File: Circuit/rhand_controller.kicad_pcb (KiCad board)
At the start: 2 copper layers, 100 x 100 mm, 39 parts, among them P1 BLUETOOTH, P10 LV_ADC, P11 LW_ADC, P12 RU_ADC, P13 RV_ADC, P14 RW_ADC, P2 CONN_01X06, P3 Wall, P4 CW, P5 Enable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

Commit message: 実態配線図完了
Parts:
- moved D1 10.2 mm to (83.0, 104.7), turned to 270 degrees
- moved R5 8.90 mm to (90.5, 110.4), turned to 180 degrees
- moved P2 2.67 mm to (79.8, 74.0)
- moved R7 2.05 mm to (105.0, 124.5)
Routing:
- net GND: track 418.2 -> 558.3 mm
- net +3V3: track 358.1 -> 386.8 mm, vias 0 -> 2
- net Net-(R5-Pad1): track 0.11 -> 4.50 mm
- net /SWDIO: track 0.00 -> 3.63 mm
- net Net-(D1-Pad2): track 0.00 -> 3.22 mm
- net /SWO: track 0.00 -> 2.96 mm
- net /315MHz_RXD: track 0.00 -> 2.20 mm
- net /NRST: track 4.76 -> 6.84 mm
- added copper zone on B.Cu, net /NRST
- added copper zone on B.Cu, net /SWCLK

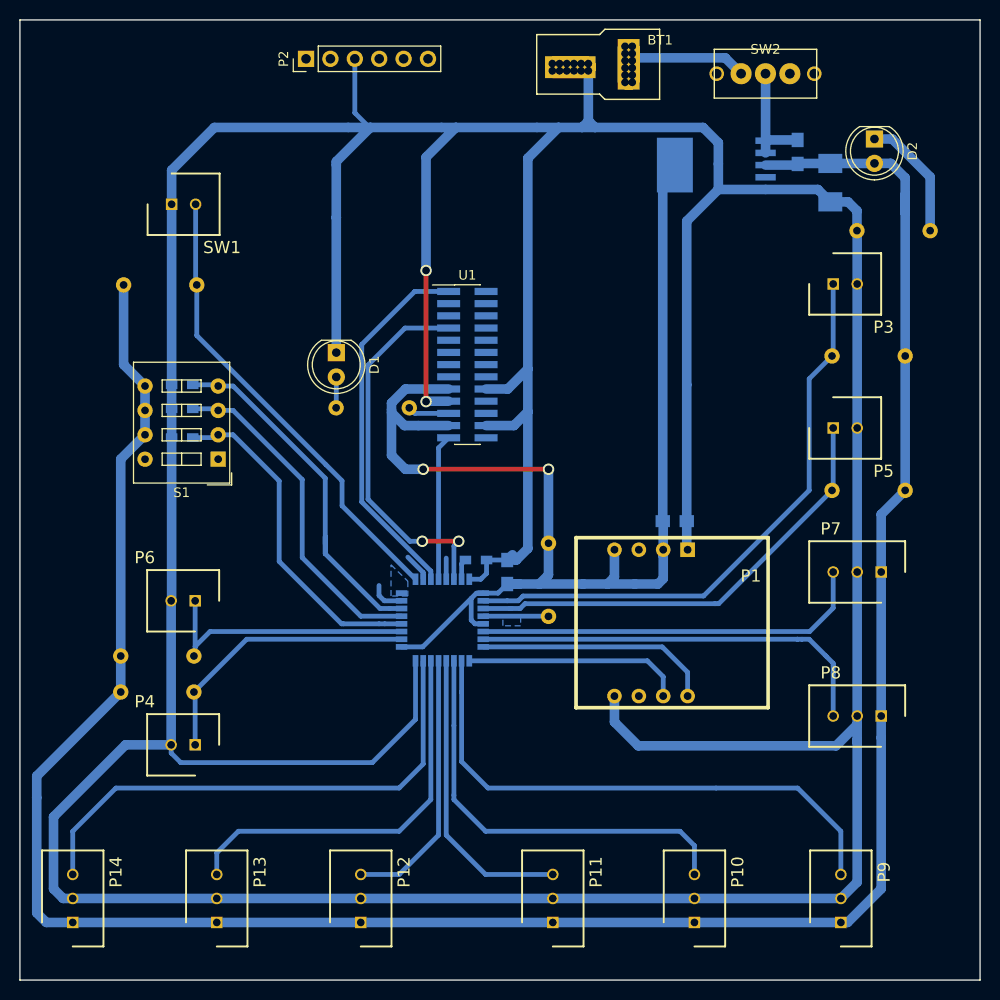
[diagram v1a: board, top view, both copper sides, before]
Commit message: SWDのジャンパ用配線の追加とガーバーデータの作製
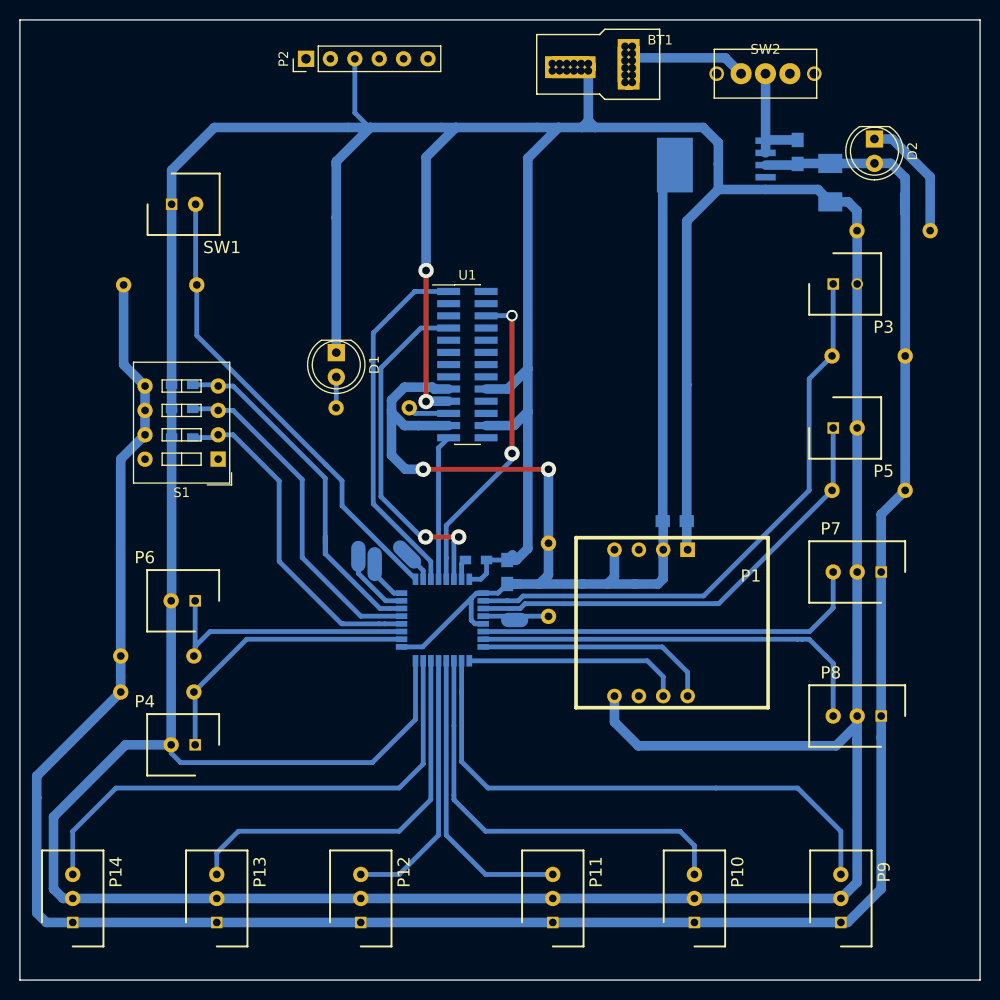
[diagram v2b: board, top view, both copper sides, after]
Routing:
- net /315MHz_RXD: track 2.20 -> 33.0 mm, vias 0 -> 2
- net /SWCLK: track 0.00 -> 5.68 mm
- net /SWDIO: track 3.63 -> 8.33 mm
- net /315MHz_TXD: track 39.4 -> 36.6 mm
- net /NRST: track 6.84 -> 8.59 mm
- net /SWO: track 2.96 -> 4.29 mm
- net /busy: track 38.8 -> 37.8 mm
- removed copper zone on B.Cu, net /NRST
- removed copper zone on B.Cu, net /SWCLK
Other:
- net class Default: via_dia 1.2 -> 1.6
